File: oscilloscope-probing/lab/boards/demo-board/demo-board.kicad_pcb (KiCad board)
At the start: 8 copper layers, 126 x 117 mm, 303 parts, among them J1 CONN_01X03, J10 SMA-J-P-H-ST-EM1, J11 TESTCLIP, J12 TESTCLIP, J13 TESTCLIP, J14 USB_C_Receptacle_USB2.0, J15 TESTCLIP, J16 SMA-J-P-H-ST-EM1, J17 SMA-J-P-H-ST-EM1, J18 SMA-J-P-H-ST-EM1, J19 SMA-J-P-H-ST-EM1, J2 CORTEX_DEBUG_ETM, J20 SMA-J-P-H-ST-EM1, J21 SMA-J-P-H-ST-EM1, J22 SMA-J-P-H-ST-EM1, J23 SMA-J-P-H-ST-EM1, J24 PMOD_HOST, J3 XILINX_JTAG, J4 CORTEX_DEBUG_ETM, J5 DISPLAY, J6 CONN_01X06, J7 SMA-J-P-H-ST-EM1, J8 SMA-J-P-H-ST-EM1, J9 SMA-J-P-H-ST-EM1, M1 LOGO, M2 LOGO, M3 LOGO, M4 LOGO, Q1 SSM6N58NU, SW1 SWITCH, SW2 SWITCH, SW3 SWITCH, SW4 SWITCH, SW5 SWITCH, SW6 SWITCH, SW7 SWITCH, U1 FT234XD, U10 19-C47/RSGHBHC-5V01/2T, U11 19-C47/RSGHBHC-5V01/2T, U12 19-C47/RSGHBHC-5V01/2T, U13 19-C47/RSGHBHC-5V01/2T, U2 STM32L431-QFN48, U26 74LVC1T45, U3 LTC3374A, U39 NCP45525IMNTWG-H, U4 XC7A35T-2FGG484I, U5 STM32H750XBH6, U6 ECS-1612MV-250-CN, U7 ECS-1612MV-250-CN, U8 S25FL064LABMFI013, U9 SIT9121AI-2BF-XXS156.250000G

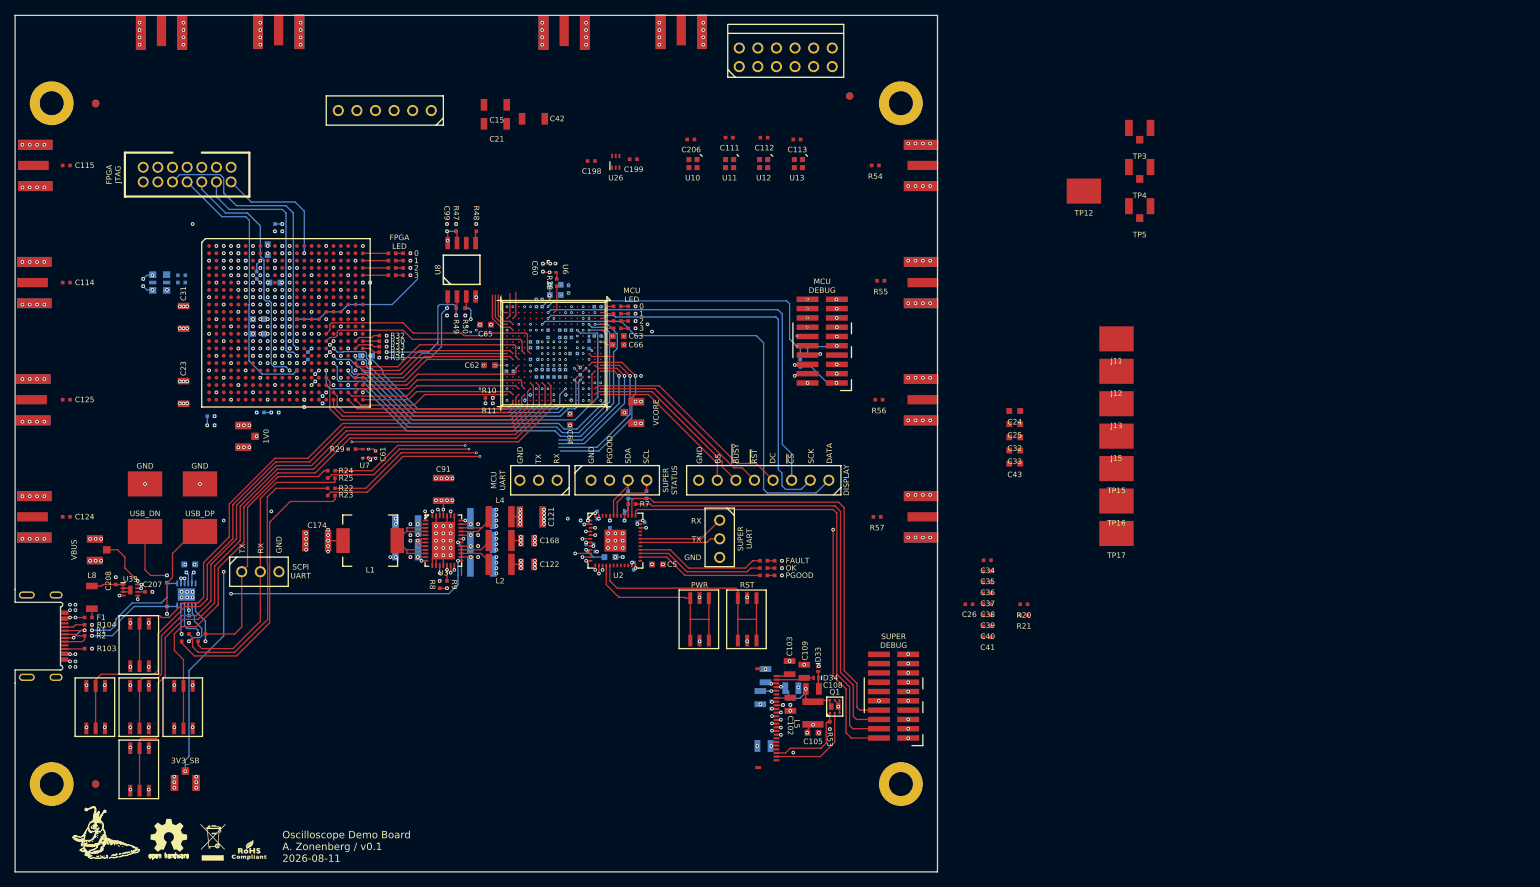
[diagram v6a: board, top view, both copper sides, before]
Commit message: Under 100 unrouted
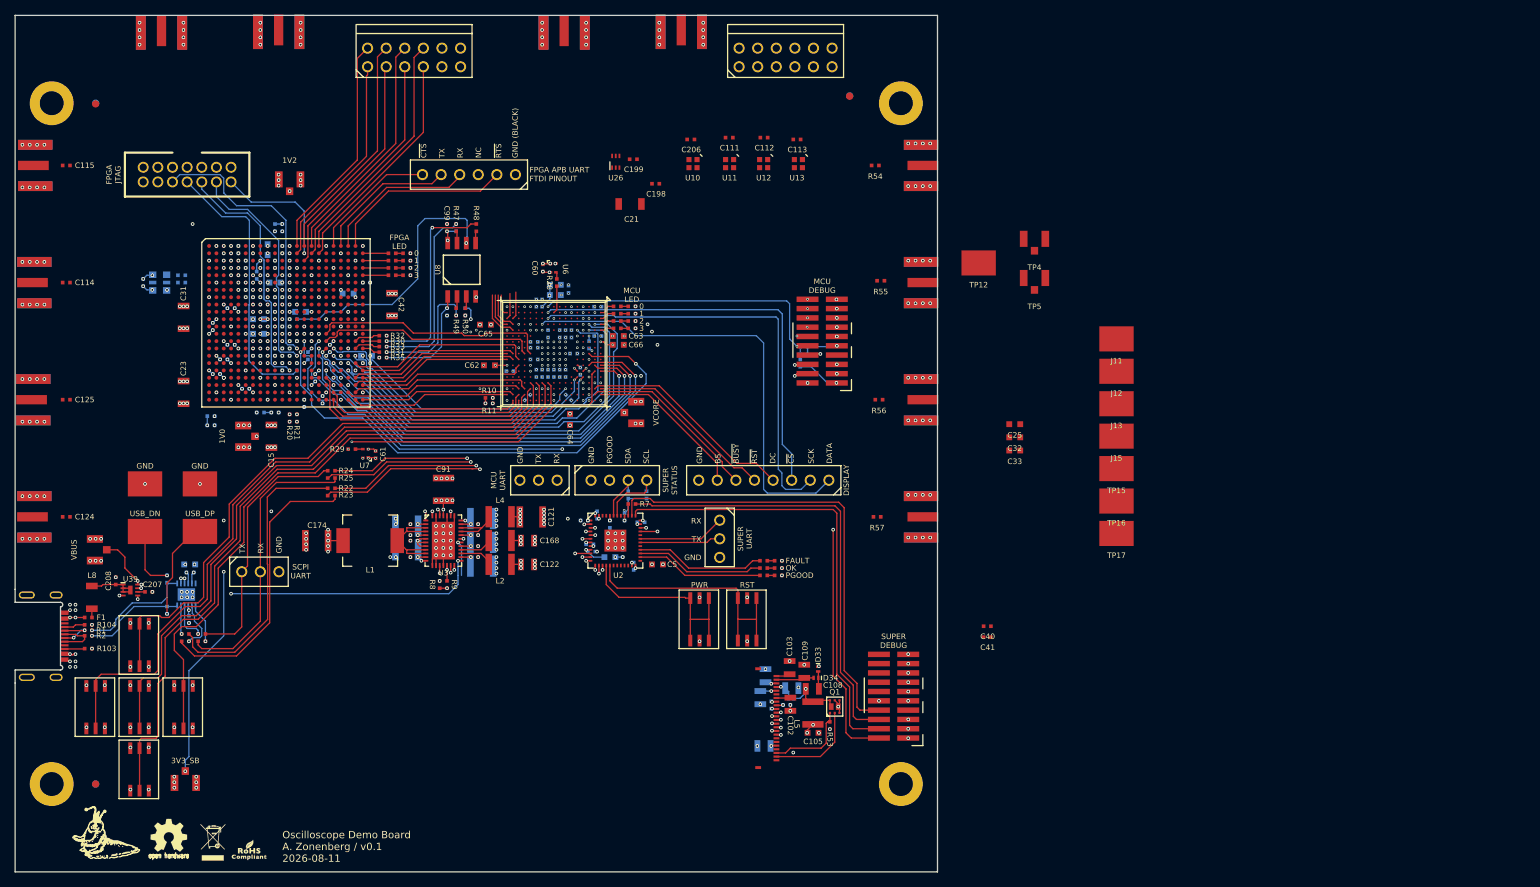
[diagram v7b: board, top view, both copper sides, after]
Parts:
- added J25: PMOD_HOST, azonenberg_pcb:CONN_HEADER_2.54MM_2x6_RA_PMOD_HOST, F.Cu at (80.5, 29.8)
- C24, C26, C34, C35, C36, C37, C38, C39, C43: moved to B.Cu
- moved TP3 116.3 mm to (63.5, 46.5)
- moved C35 111.0 mm to (53.0, 66.5), turned to 90 degrees
- moved C37 110.4 mm to (55.5, 64.0)
- moved C39 109.7 mm to (55.5, 69.0), turned to 180 degrees
- moved C36 108.7 mm to (54.5, 71.0)
- moved C34 108.3 mm to (53.5, 73.0), turned to 180 degrees
- moved C38 105.5 mm to (57.5, 75.0), turned to 180 degrees
- moved R20 103.5 mm to (63.5, 79.0), turned to -90 degrees
- moved C26 103.3 mm to (61.0, 64.5), turned to 180 degrees
- moved R21 102.9 mm to (64.5, 79.0), turned to -90 degrees
- moved C24 98.5 mm to (65.0, 64.5)
- moved C43 94.0 mm to (71.5, 62.0)
- moved C15 54.7 mm to (61.0, 81.5), turned to 90 degrees
- moved C42 31.9 mm to (77.5, 63.5), turned to -90 degrees
- moved C21 21.4 mm to (110.0, 49.8)
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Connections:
- J6 pad 2: /Test signals/FPGA_UART_CTS_N -> /Test signals/FPGA_UART_RTS_N
- J6 pad 4: /Test signals/FPGA_UART_TX -> /Test signals/FPGA_UART_RX
- J6 pad 5: /Test signals/FPGA_UART_RX -> /Test signals/FPGA_UART_TX
- J6 pad 6: /Test signals/FPGA_UART_RTS_N -> /Test signals/FPGA_UART_CTS_N
- U4 pad A13: unconnected-(U4F-IO_L10P_T1_16-PadA13) -> /Test signals/FPGA_PMOD_DQ4
- U4 pad A14: unconnected-(U4F-IO_L10N_T1_16-PadA14) -> /Test signals/FPGA_PMOD_DQ5
- U4 pad A15: unconnected-(U4F-IO_L9P_T1_DQS_16-PadA15) -> /Test signals/FPGA_PMOD_DQ6
- U4 pad A16: unconnected-(U4F-IO_L9N_T1_DQS_16-PadA16) -> /Test signals/FPGA_PMOD_DQ7
- U4 pad A20: /Test signals/FPGA_UART_RTS_N -> /Test signals/FPGA_UART_RX
- U4 pad A21: /Test signals/FPGA_UART_RX -> /Test signals/FPGA_UART_RTS_N
- U4 pad B13: unconnected-(U4F-IO_L8N_T1_16-PadB13) -> /Test signals/FPGA_PMOD_DQ0
- U4 pad B15: unconnected-(U4F-IO_L7P_T1_16-PadB15) -> /Test signals/FPGA_PMOD_DQ2
- U4 pad B16: unconnected-(U4F-IO_L7N_T1_16-PadB16) -> /Test signals/FPGA_PMOD_DQ3
- U4 pad C14: unconnected-(U4F-IO_L3P_T0_DQS_16-PadC14) -> /Test signals/FPGA_PMOD_DQ1
- U4 pad P16: /MCU/FMC_NOE -> /MCU/FMC_NE1
- U4 pad R14: /MCU/FMC_NE1 -> /MCU/FMC_NE4
- U4 pad R16: /MCU/FMC_NWAIT -> /MCU/FMC_NWE
- U4 pad R17: /MCU/FMC_NE4 -> /MCU/FMC_NBL1
- U4 pad U17: /MCU/FMC_NWE -> /MCU/FMC_NOE
- U4 pad V17: /MCU/FMC_NBL1 -> /MCU/FMC_NWAIT
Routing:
- net /FPGA support/1V8: track 91.7 -> 160.2 mm, vias 30 -> 37
- net /MCU/FMC_NE4: track 3.57 -> 71.1 mm, vias 0 -> 2
- net /MCU/FMC_AD3: track 0.57 -> 57.9 mm, vias 1 -> 3
- net /MCU/FMC_NE1: track 24.9 -> 65.7 mm, vias 1 -> 2
- net /MCU/MCU_BOOT0: track 0.00 -> 39.6 mm, vias 1 -> 3
- net /GND: track 1273.0 -> 1311.3 mm, vias 454 -> 472
- net /MCU/FMC_NWE: track 21.5 -> 59.6 mm, vias 1 -> 2
- net /MCU/FMC_NOE: track 16.8 -> 52.2 mm, vias 1 -> 2
- net /MCU/FMC_NWAIT: track 19.7 -> 54.6 mm, vias 1 -> 2
- net /Test signals/FPGA_PMOD_DQ7: track 0.00 -> 32.9 mm
- net /Test signals/FPGA_PMOD_DQ6: track 0.00 -> 32.3 mm
- net /Test signals/FPGA_PMOD_DQ5: track 0.00 -> 31.7 mm
- net /Test signals/FPGA_PMOD_DQ3: track 0.00 -> 31.4 mm
- net /Test signals/FPGA_PMOD_DQ1: track 0.00 -> 31.1 mm
- net /Test signals/FPGA_PMOD_DQ4: track 0.00 -> 31.0 mm
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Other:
- board text added: "1V2"
- board text added: "FPGA APB UART FTDI PINOUT"
- board text added: "GND (BLACK)"
- board text added: "NC"
- board text added: "~{CTS}"
- board text added: "~{RTS}"

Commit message: Continued layout, 55 unrouted
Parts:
- C111, C112, C113, C198, C199, C206: moved to B.Cu
- moved TP15 91.1 mm to (99.0, 38.0), turned to 90 degrees
- moved C21 54.5 mm to (65.8, 81.5), turned to 90 degrees
- moved TP12 47.6 mm to (110.0, 57.0)
- moved U13 16.7 mm to (117.2, 38.8)
- moved C113 15.7 mm to (117.2, 38.8), turned to 135 degrees
- moved U12 15.5 mm to (113.8, 38.8)
- moved C112 14.7 mm to (113.8, 38.8), turned to 135 degrees
- moved U11 14.4 mm to (110.2, 38.8)
- moved C111 13.4 mm to (110.2, 38.8), turned to 135 degrees
- moved U10 13.1 mm to (106.8, 38.8)
- moved C198 11.8 mm to (103.5, 40.8), turned to -90 degrees
- moved C206 11.8 mm to (106.8, 38.8), turned to 135 degrees
- moved C199 8.23 mm to (102.8, 40.8), turned to -90 degrees
- moved U26 7.50 mm to (102.8, 38.7), turned to 180 degrees
- turned R56 to 180 degrees
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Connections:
- U2 pad 32: /FPGA support/FPGA_RST_N -> /FPGA support/FPGA_INIT
- U2 pad 41: /FPGA support/FPGA_INIT -> /FPGA support/FPGA_RST_N
- U5 pad B17: unconnected-(U5H-PH14-PadB17) -> /MCU/MCU_DONE
- U5 pad C1: unconnected-(U5C-PC15-PadC1) -> /MCU/MCU_TRIG
- U5 pad E4: /MCU/MCU_TRIG -> unconnected-(U5I-PI8-PadE4)
- U5 pad G4: /MCU/MCU_DONE -> unconnected-(U5F-PF0-PadG4)
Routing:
- net /VBUS: track 113.7 -> 258.7 mm, vias 22 -> 27
- net /FPGA support/FPGA_INIT: track 7.41 -> 66.8 mm, vias 2 -> 3
- net /MCU/DAC1_OUT2: track 3.77 -> 58.2 mm
- net /FPGA support/FPGA_RST_N: track 11.4 -> 65.7 mm, vias 2 -> 3
- net /FPGA support/FPGA_DONE: track 15.5 -> 68.4 mm, vias 1 -> 3
- net /MCU/MCU_RST_N: track 43.4 -> 93.1 mm, vias 2 -> 3
- net /MCU/DAC1_OUT1: track 3.57 -> 43.2 mm
- net /GND: track 1311.3 -> 1344.4 mm, vias 472 -> 482
- net /MCU/FMC_AD8: track 0.00 -> 31.5 mm, vias 1 -> 2
- net /MCU/MCU_DONE: track 0.00 -> 16.4 mm
- net /MCU/MCU_TRIG: track 0.00 -> 11.8 mm
- net /3V3: track 748.7 -> 755.2 mm, vias 112 -> 114
- net /FPGA support/1V0: track 70.6 -> 75.4 mm, vias 33 -> 36
- net /Test signals/LED_CTRL_5V0: track 0.00 -> 4.78 mm
- net /Test signals/LED_CTRL: track 0.00 -> 3.29 mm
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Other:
- board text added: "3V3"
- board text added: "FPGA PMOD"
- board text added: "LED1"
- board text added: "LED2"
- board text added: "LED3"
- board text added: "LED4"
- board text added: "LED_CTRL"
- board text added: "MCU PMOD"
- board text added: "TRIG"
